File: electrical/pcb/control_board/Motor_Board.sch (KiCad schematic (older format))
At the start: 72 parts, among them J1 XT30-M, J10 Molex_172675-0613, J11 Molex_172675-0613, J12 TSW-104-07-F-T, J13 Molex_172675-0613, J14 Molex_172675-0613, J15 TSW-104-07-F-T, J16 ED2627-ND, J17 ED2627-ND, J18 ED2627-ND, J19 TSW-104-07-F-T, J2 XT30-F, J20 PEC08SAAN, J21 PPTC102LFBN-RC, J3 XT30-F, J4 XT30-F, J5 XT30-M, J6 ED2580-ND, J7 TSW-104-07-F-T, J8 Molex_172675-0613, J9 Molex_172675-0613, T1 test_point, T2 test_point, T3 test_point, T4 test_point, T5 test_point, T6 test_point, U1 INA260, U2 PCA9685, U3 D24V22Fx, U4 D24V150Fx, U5 DC7G3HWA, y1 rover_silkscreen

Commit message: Finished rev2 layout for motor board
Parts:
- added MH5, MH6, MH7, MH8: #6THRU-HOLE, JPL Robotics:#6THRU-HOLE, symbol JPL_Robotics_Lib:#6THRU-HOLE
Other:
- note added: "For mounting brain board"
- note added: "For mounting to to \nrover structure"
- moved on the sheet: MH1, MH2, MH3, MH4
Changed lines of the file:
@@
 L JPL_Robotics_Lib:#6THRU-HOLE MH1
 U 1 1 60953101
-P 2250 8850
-F 0 "MH1" H 2381 8850 30  0000 L CNN
-F 1 "#6THRU-HOLE" H 2250 8990 30  0001 C CNN
-F 2 "JPL Robotics:#6THRU-HOLE" H 2250 8940 30  0001 C CNN
-F 3 "" H 2250 8940 30  0001 C CNN
-	1    2250 8850
+P 1450 8900
+F 0 "MH1" H 1581 8900 30  0000 L CNN
+F 1 "#6THRU-HOLE" H 1450 9040 30  0001 C CNN
+F 2 "JPL Robotics:#6THRU-HOLE" H 1450 8990 30  0001 C CNN
+F 3 "" H 1450 8990 30  0001 C CNN
+	1    1450 8900
 	1    0    0    -1
 $EndComp
@@
 L JPL_Robotics_Lib:#6THRU-HOLE MH2
 U 1 1 60953107
-P 2250 9000
-F 0 "MH2" H 2381 9000 30  0000 L CNN
-F 1 "#6THRU-HOLE" H 2250 9140 30  0001 C CNN
-F 2 "JPL Robotics:#6THRU-HOLE" H 2250 9090 30  0001 C CNN
-F 3 "" H 2250 9090 30  0001 C CNN
-	1    2250 9000
+P 1450 9050
+F 0 "MH2" H 1581 9050 30  0000 L CNN
+F 1 "#6THRU-HOLE" H 1450 9190 30  0001 C CNN
+F 2 "JPL Robotics:#6THRU-HOLE" H 1450 9140 30  0001 C CNN
+F 3 "" H 1450 9140 30  0001 C CNN
+	1    1450 9050
 	1    0    0    -1
 $EndComp
@@
 L JPL_Robotics_Lib:#6THRU-HOLE MH3
 U 1 1 6095310D
-P 2250 9150
-F 0 "MH3" H 2381 9150 30  0000 L CNN
-F 1 "#6THRU-HOLE" H 2250 9290 30  0001 C CNN
-F 2 "JPL Robotics:#6THRU-HOLE" H 2250 9240 30  0001 C CNN
-F 3 "" H 2250 9240 30  0001 C CNN
-	1    2250 9150
+P 1450 9200
+F 0 "MH3" H 1581 9200 30  0000 L CNN
+F 1 "#6THRU-HOLE" H 1450 9340 30  0001 C CNN
+F 2 "JPL Robotics:#6THRU-HOLE" H 1450 9290 30  0001 C CNN
+F 3 "" H 1450 9290 30  0001 C CNN
+	1    1450 9200
 	1    0    0    -1
 $EndComp
@@
 L JPL_Robotics_Lib:#6THRU-HOLE MH4
 U 1 1 60953113
-P 2250 9300
-F 0 "MH4" H 2381 9300 30  0000 L CNN
-F 1 "#6THRU-HOLE" H 2250 9440 30  0001 C CNN
-F 2 "JPL Robotics:#6THRU-HOLE" H 2250 9390 30  0001 C CNN
-F 3 "" H 2250 9390 30  0001 C CNN
-	1    2250 9300
+P 1450 9350
+F 0 "MH4" H 1581 9350 30  0000 L CNN
+F 1 "#6THRU-HOLE" H 1450 9490 30  0001 C CNN
+F 2 "JPL Robotics:#6THRU-HOLE" H 1450 9440 30  0001 C CNN
+F 3 "" H 1450 9440 30  0001 C CNN
+	1    1450 9350
 	1    0    0    -1
 $EndComp
@@
 NoConn ~ 14250 6500
 NoConn ~ 14250 6600
+$Comp
+L JPL_Robotics_Lib:#6THRU-HOLE MH5
+U 1 1 625AC662
+P 2350 8900
+F 0 "MH5" H 2481 8900 30  0000 L CNN
+F 1 "#6THRU-HOLE" H 2350 9040 30  0001 C CNN
+F 2 "JPL Robotics:#6THRU-HOLE" H 2350 8990 30  0001 C CNN
+F 3 "" H 2350 8990 30  0001 C CNN
+	1    2350 8900
+	1    0    0    -1
+$EndComp
+$Comp
+L JPL_Robotics_Lib:#6THRU-HOLE MH6
+U 1 1 625AC668
+P 2350 9050
+F 0 "MH6" H 2481 9050 30  0000 L CNN
+F 1 "#6THRU-HOLE" H 2350 9190 30  0001 C CNN
+F 2 "JPL Robotics:#6THRU-HOLE" H 2350 9140 30  0001 C CNN
+F 3 "" H 2350 9140 30  0001 C CNN
+	1    2350 9050
+	1    0    0    -1
+$EndComp
+$Comp
+L JPL_Robotics_Lib:#6THRU-HOLE MH7
+U 1 1 625AC66E
+P 2350 9200
+F 0 "MH7" H 2481 9200 30  0000 L CNN
+F 1 "#6THRU-HOLE" H 2350 9340 30  0001 C CNN
+F 2 "JPL Robotics:#6THRU-HOLE" H 2350 9290 30  0001 C CNN
+F 3 "" H 2350 9290 30  0001 C CNN
+	1    2350 9200
+	1    0    0    -1
+$EndComp
+$Comp
+L JPL_Robotics_Lib:#6THRU-HOLE MH8
+U 1 1 625AC674
+P 2350 9350
+F 0 "MH8" H 2481 9350 30  0000 L CNN
+F 1 "#6THRU-HOLE" H 2350 9490 30  0001 C CNN
+F 2 "JPL Robotics:#6THRU-HOLE" H 2350 9440 30  0001 C CNN
+F 3 "" H 2350 9440 30  0001 C CNN
+	1    2350 9350
+	1    0    0    -1
+$EndComp
+Text Notes 1250 8800 0    31   ~ 0
+For mounting to to \nrover structure
+Text Notes 2100 8800 0    31   ~ 0
+For mounting brain board
 $EndSCHEMATC

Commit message: Some small updates before final routing
- Routed 12V_EN line to rpi
- A bunch of schematic cleanup
- Switched ESTOP LEDs to 5v from 3.3v
- Updated LED resistor sizing
- Connected available LEDs to unused rpi GPIOse
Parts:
- added R21: 0, symbol Device:R
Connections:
- wire segments 396 -> 398
- no-connect marks 67 -> 66
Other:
- note added: "Corner Steering \nServos Header"
- note added: "EN is pulled up by default on the \nD24V22F12, enabling it. Connect \nEN directly to RPi, so RPi can drive \nthis pin low and disable 12V output. \n\nThis resistor is a depop-able, just \nin case"
- note added: "Extra PWM Outputs Headers"
- note added: "Note: laid out the pins on this connector so that \nit wouldn’t be disastrous if the direction was \naccidentally switched"
- note added: "Note: leaving these unconnected, and \nsupplying +5V directly from the 5V bus"
- note added: "These are decoupling caps for the servos"
- note removed: "I think these are staying unconnected"
- note removed: "TODO: make sure to place this interboard connector such that no one will ever fuck up the direction this is plugged in"
- note removed: "TODO: think about A vs U naming convention"
- note removed: "TODO: tie EN pin for 12v reg to pin on the rpi. Also add a pull down for this\n\nEric to look into what we want to do here"
- note removed: "These are decoupling caps for the servos \n(todo: put as close to servos as possible in board layout)"
- moved on the sheet: C19, J19, J21, R10, R6, R7, R8, R9, U5

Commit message: Updates to layout
- Placed 12V_enable line in layout
- Placed additional LED resistors in layout
- Placed testpoints in layout
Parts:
- removed T5: test_point, TestPoint:TestPoint_Pad_1.0x1.0mm, symbol JPL_Robotics_Lib:test_point
- R2, R3, R4: symbol Device:R -> Device:R_US
- R21: footprint (none) -> Resistor_THT:R_Axial_DIN0207_L6.3mm_D2.5mm_P7.62mm_Horizontal; symbol Device:R -> Device:R_US
- renumbered T6 to T5
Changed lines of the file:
@@
 P 14650 9000
 AR Path="/60B753B5" Ref="T?"  Part="1"
-AR Path="/60A51BAC/60B753B5" Ref="T6"  Part="1"
-F 0 "T6" V 14650 8900 30  0000 L CNN
+AR Path="/60A51BAC/60B753B5" Ref="T5"  Part="1"
+F 0 "T5" V 14650 8900 30  0000 L CNN
 F 1 "test_point" H 14800 9250 50  0001 C CNN
 F 2 "TestPoint:TestPoint_Pad_1.0x1.0mm" H 14600 8950 50  0001 C CNN
@@
 Pulllups for e_stop signals
 $Comp
-L Device:R R2
+L Device:R_US R2
 U 1 1 61145EF5
 P 3150 3650
@@
 $EndComp
 $Comp
-L Device:R R3
+L Device:R_US R3
 U 1 1 6115BE1A
 P 3450 3650
@@
 $EndComp
 $Comp
-L Device:R R4
+L Device:R_US R4
 U 1 1 6115C337
 P 3750 3650
@@
 	1    13250 7650
 	1    0    0    -1
-$EndComp
-$Comp
-L JPL_Robotics_Lib:test_point T?
-U 1 1 6123BED4
-P 13200 9500
-AR Path="/6123BED4" Ref="T?"  Part="1"
-AR Path="/60A51BAC/6123BED4" Ref="T5"  Part="1"
-F 0 "T5" H 13150 9450 30  0000 L CNN
-F 1 "test_point" H 13350 9750 50  0001 C CNN
-F 2 "TestPoint:TestPoint_Pad_1.0x1.0mm" H 13150 9450 50  0001 C CNN
-F 3 "" H 13150 9450 50  0001 C CNN
-	1    13200 9500
-	-1   0    0    1
 $EndComp
 Text Notes 13750 5250 0    98   ~ 0
@@
 Wire Wire Line
 	14650 9150 14800 9150
-Connection ~ 13350 9500
 NoConn ~ 14500 9300
 Wire Wire Line
@@
 For mounting brain board
 $Comp
-L Device:R R21
+L Device:R_US R21
 U 1 1 62A1852A
 P 13200 9300
 F 0 "R21" V 12993 9300 50  0000 C CNN
 F 1 "0" V 13084 9300 50  0000 C CNN
-F 2 "" V 13130 9300 50  0001 C CNN
+F 2 "Resistor_THT:R_Axial_DIN0207_L6.3mm_D2.5mm_P7.62mm_Horizontal" V 13130 9300 50  0001 C CNN
 F 3 "~" H 13200 9300 50  0001 C CNN
 	1    13200 9300

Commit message: Add 277-11404-ND
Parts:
- J16, J17, J18: value ED2627-ND -> 277-11404-ND
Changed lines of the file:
@@
 AR Path="/60A51BAC/60B1CB30" Ref="J18"  Part="1"
 F 0 "J18" H 11050 3000 39  0000 L CNN
-F 1 "ED2627-ND" H 10919 3384 50  0001 C CNN
+F 1 "277-11404-ND" H 10919 3384 50  0001 C CNN
 F 2 "JPL Robotics:277-11404-ND" H 10800 3400 50  0001 C CNN
 F 3 "" H 10800 3400 50  0001 C CNN
@@
 AR Path="/60A51BAC/60B1CB18" Ref="J17"  Part="1"
 F 0 "J17" H 11050 2650 39  0000 L CNN
-F 1 "ED2627-ND" H 10919 3034 50  0001 C CNN
+F 1 "277-11404-ND" H 10919 3034 50  0001 C CNN
 F 2 "JPL Robotics:277-11404-ND" H 10800 3050 50  0001 C CNN
 F 3 "" H 10800 3050 50  0001 C CNN
@@
 AR Path="/60A51BAC/60B1CB0E" Ref="J16"  Part="1"
 F 0 "J16" H 11100 2300 39  0000 C CNN
-F 1 "ED2627-ND" H 10919 2684 50  0001 C CNN
+F 1 "277-11404-ND" H 10919 2684 50  0001 C CNN
 F 2 "JPL Robotics:277-11404-ND" H 10800 2700 50  0001 C CNN
 F 3 "" H 10800 2700 50  0001 C CNN

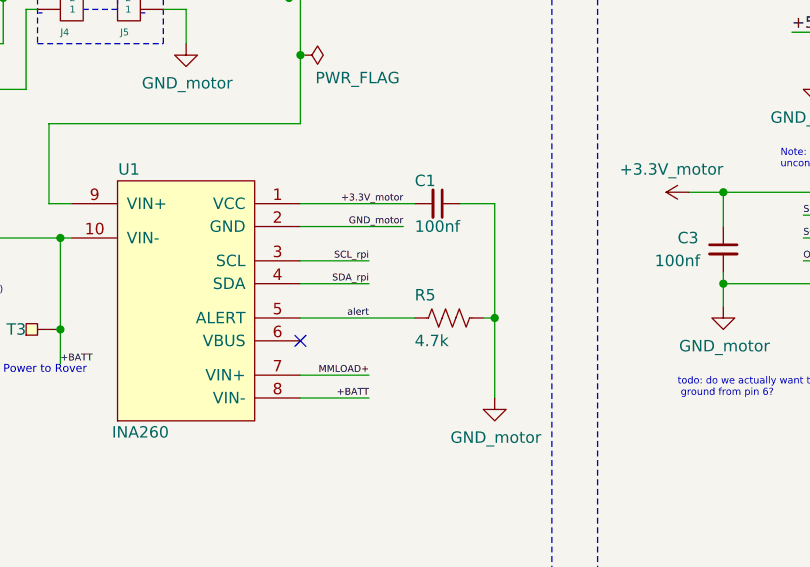
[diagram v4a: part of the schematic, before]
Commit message: Moved alert from pull-down to +3.3V pull-up
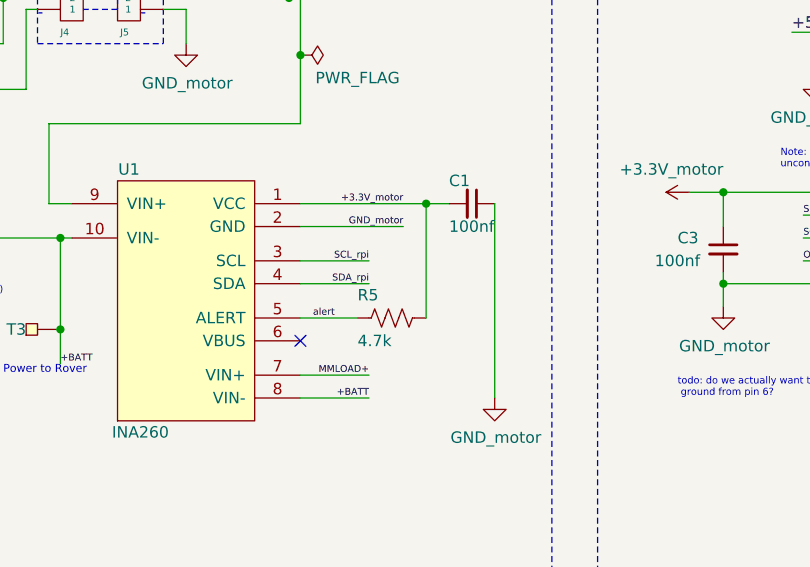
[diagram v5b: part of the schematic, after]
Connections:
- net +3.3V_motor: now also R5.1
- net GND_motor: no longer R5.1
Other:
- moved on the sheet: C1, R5
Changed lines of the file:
@@
 Wire Wire Line
 	3800 6800 4100 6800
-Wire Wire Line
-	4650 7050 4650 7400
-Wire Wire Line
-	4600 7050 4650 7050
-Wire Wire Line
-	4650 6550 4650 7050
-Wire Wire Line
-	4500 6550 4650 6550
-Wire Wire Line
-	3800 7050 4300 7050
-Wire Wire Line
-	3800 6550 4300 6550
 $Comp
 L JPL_Robotics_Lib:GND_motor #PWR06
@@
 L Device:C_Small C?
 U 1 1 61378A2A
-P 4400 6550
+P 4550 6550
 AR Path="/60A5279E/61378A2A" Ref="C?"  Part="1"
 AR Path="/60A51BAC/61378A2A" Ref="C1"  Part="1"
-F 0 "C1" V 4300 6450 50  0000 L CNN
-F 1 "100nf" V 4500 6450 50  0000 L CNN
-F 2 "Resistor_THT:R_Axial_DIN0207_L6.3mm_D2.5mm_P7.62mm_Horizontal" H 4400 6550 50  0001 C CNN
-F 3 "~" H 4400 6550 50  0001 C CNN
-	1    4400 6550
+F 0 "C1" V 4450 6450 50  0000 L CNN
+F 1 "100nf" V 4650 6450 50  0000 L CNN
+F 2 "Resistor_THT:R_Axial_DIN0207_L6.3mm_D2.5mm_P7.62mm_Horizontal" H 4550 6550 50  0001 C CNN
+F 3 "~" H 4550 6550 50  0001 C CNN
+	1    4550 6550
 	0    1    1    0
 $EndComp
@@
 L Device:R_US R?
 U 1 1 613B820D
-P 4450 7050
+P 4200 7050
 AR Path="/613B820D" Ref="R?"  Part="1"
 AR Path="/60A51BAC/613B820D" Ref="R5"  Part="1"
-F 0 "R5" V 4350 6900 50  0000 L CNN
-F 1 "4.7k" V 4550 6900 50  0000 L CNN
-F 2 "Resistor_THT:R_Axial_DIN0207_L6.3mm_D2.5mm_P7.62mm_Horizontal" V 4490 7040 50  0001 C CNN
-F 3 "~" H 4450 7050 50  0001 C CNN
-	1    4450 7050
+F 0 "R5" V 4100 6900 50  0000 L CNN
+F 1 "4.7k" V 4300 6900 50  0000 L CNN
+F 2 "Resistor_THT:R_Axial_DIN0207_L6.3mm_D2.5mm_P7.62mm_Horizontal" V 4240 7040 50  0001 C CNN
+F 3 "~" H 4200 7050 50  0001 C CNN
+	1    4200 7050
 	0    1    1    0
 $EndComp
 Text Label 4250 6550 2    30   ~ 0
 +3.3V_motor
-Text Label 4100 7050 2    30   ~ 0
+Text Label 3950 7050 2    30   ~ 0
 alert
 Text Label 4100 6900 2    30   ~ 0
@@
 Wire Wire Line
 	3300 5850 3300 5700
-Connection ~ 4650 7050
 Wire Wire Line
 	1900 6550 1900 6850
@@
 Wire Notes Line
 	12100 9900 12100 7000
+Wire Wire Line
+	4650 6550 4650 7400
+Wire Wire Line
+	4050 7050 3800 7050
+Wire Wire Line
+	3800 6550 4350 6550
+Wire Wire Line
+	4350 7050 4350 6550
+Connection ~ 4350 6550
+Wire Wire Line
+	4350 6550 4450 6550
 $EndSCHEMATC

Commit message: Update c19, c25, c27, c28 to polarized footprint
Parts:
- C19, C25, C27, C28: footprint Resistor_THT:R_Axial_DIN0207_L6.3mm_D2.5mm_P7.62mm_Horizontal -> Capacitor_THT:CP_Radial_D8.0mm_P3.80mm
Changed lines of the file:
@@
 F 0 "C19" V 9400 6250 50  0000 L CNN
 F 1 "100uf" V 9200 6250 50  0000 L CNN
-F 2 "Resistor_THT:R_Axial_DIN0207_L6.3mm_D2.5mm_P7.62mm_Horizontal" H 9300 6300 50  0001 C CNN
+F 2 "Capacitor_THT:CP_Radial_D8.0mm_P3.80mm" H 9300 6300 50  0001 C CNN
 F 3 "~" H 9300 6300 50  0001 C CNN
 	1    9300 6300
@@
 F 0 "C25" V 10250 9400 50  0000 L CNN
 F 1 "100uf" V 10050 9400 50  0000 L CNN
-F 2 "Resistor_THT:R_Axial_DIN0207_L6.3mm_D2.5mm_P7.62mm_Horizontal" H 10150 9450 50  0001 C CNN
+F 2 "Capacitor_THT:CP_Radial_D8.0mm_P3.80mm" H 10150 9450 50  0001 C CNN
 F 3 "~" H 10150 9450 50  0001 C CNN
 	1    10150 9450
@@
 F 0 "C27" V 10550 9400 50  0000 L CNN
 F 1 "100uf" V 10350 9400 50  0000 L CNN
-F 2 "Resistor_THT:R_Axial_DIN0207_L6.3mm_D2.5mm_P7.62mm_Horizontal" H 10450 9450 50  0001 C CNN
+F 2 "Capacitor_THT:CP_Radial_D8.0mm_P3.80mm" H 10450 9450 50  0001 C CNN
 F 3 "~" H 10450 9450 50  0001 C CNN
 	1    10450 9450
@@
 F 0 "C28" V 10850 9400 50  0000 L CNN
 F 1 "100uf" V 10650 9400 50  0000 L CNN
-F 2 "Resistor_THT:R_Axial_DIN0207_L6.3mm_D2.5mm_P7.62mm_Horizontal" H 10750 9450 50  0001 C CNN
+F 2 "Capacitor_THT:CP_Radial_D8.0mm_P3.80mm" H 10750 9450 50  0001 C CNN
 F 3 "~" H 10750 9450 50  0001 C CNN
 	1    10750 9450

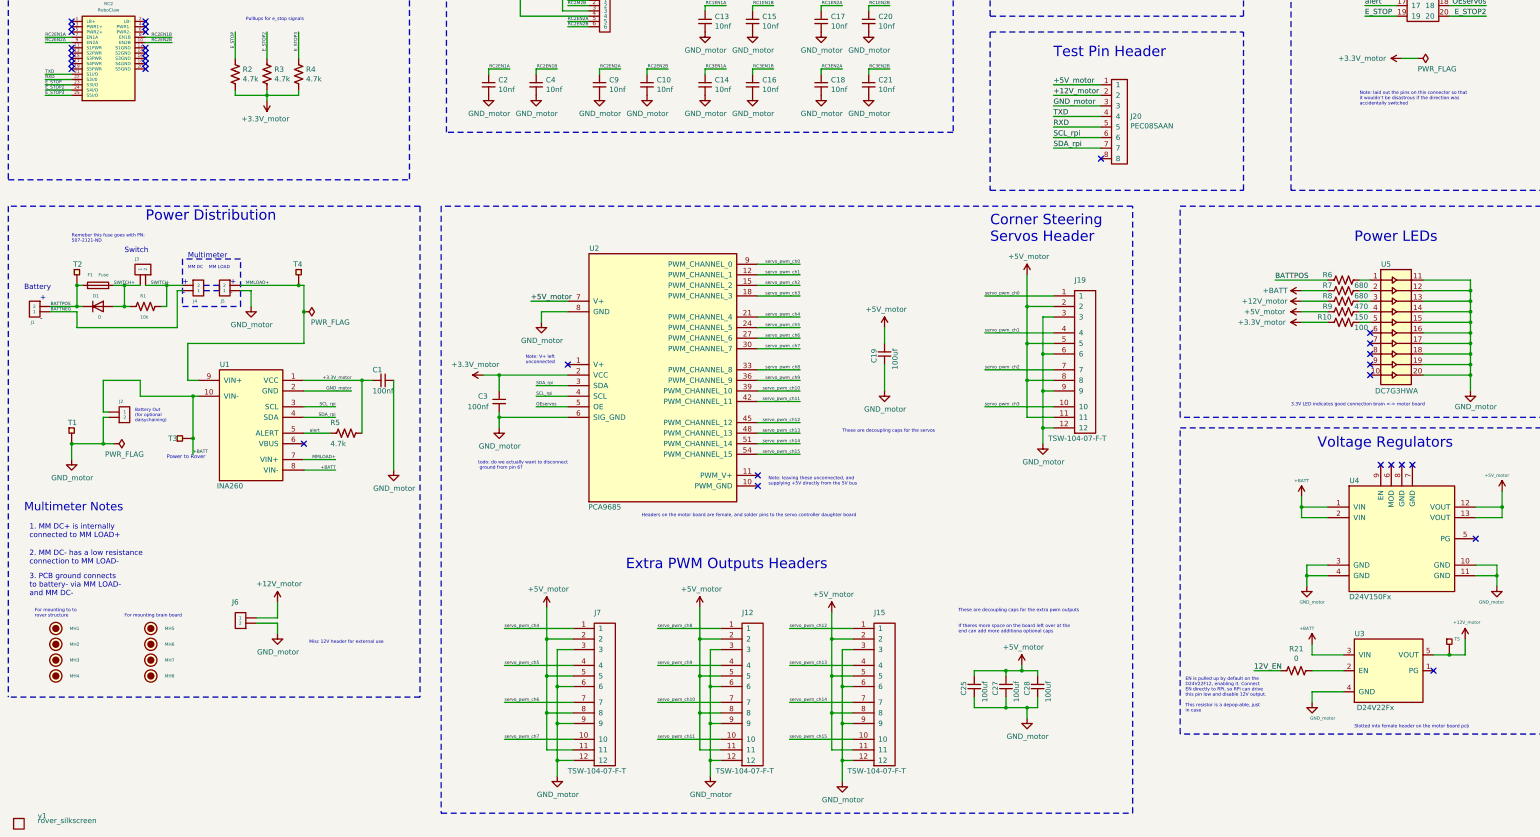
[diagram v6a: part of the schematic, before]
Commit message: Refactor the test points, in particular added an array of test points for motor board. Add a couple of bigger test point footprints as well
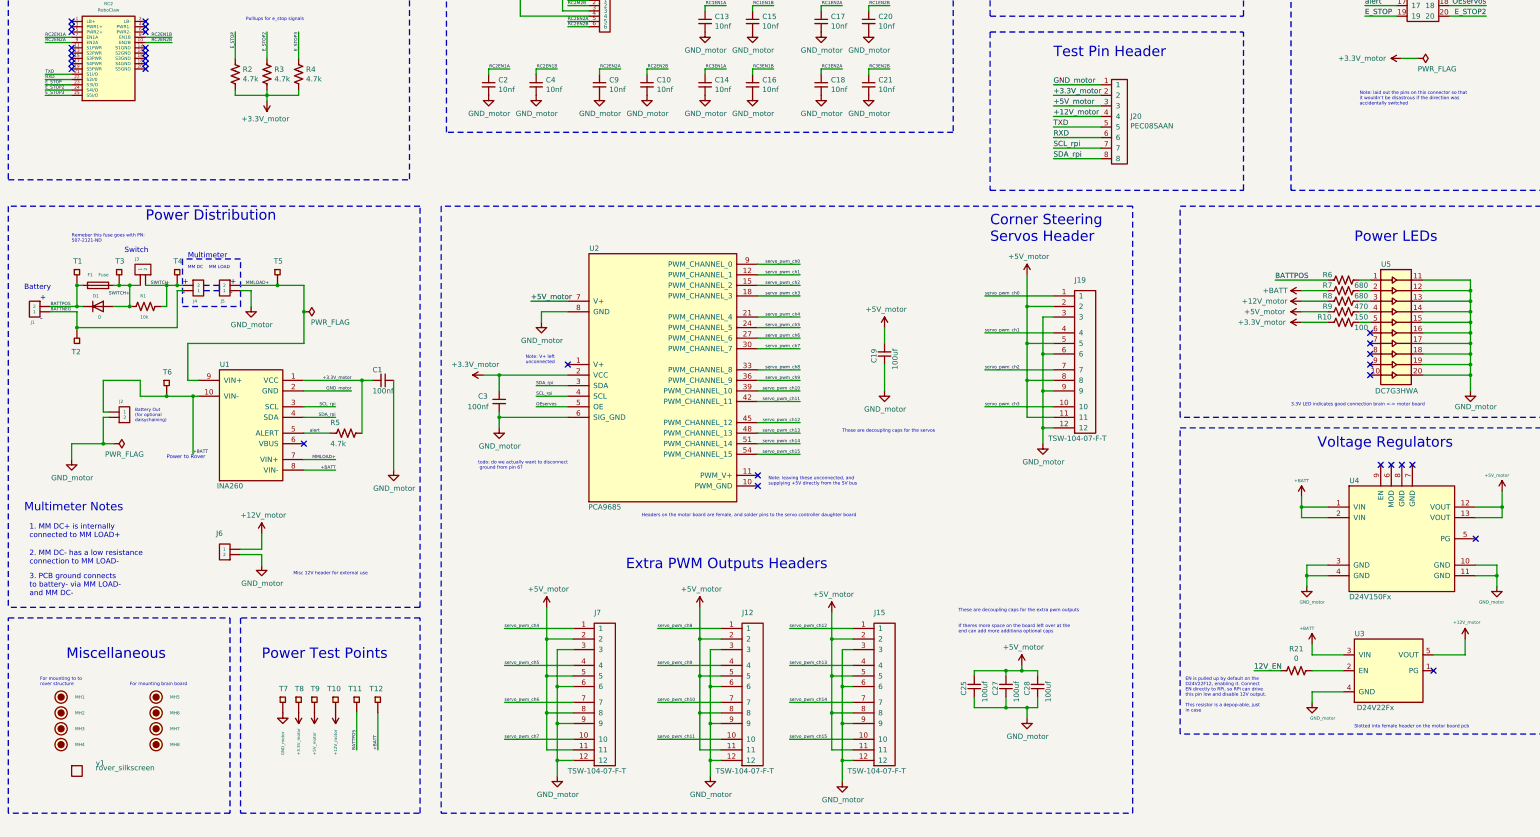
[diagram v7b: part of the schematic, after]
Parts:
- added T10, T11, T12, T8, T9: JPL Robotics:test_point_hole, symbol JPL_Robotics_Lib:test_point
- added T6: test_point, JPL Robotics:test_point, symbol JPL_Robotics_Lib:test_point
- added T7: test_point, JPL Robotics:test_point_hole, symbol JPL_Robotics_Lib:test_point
- T1, T2: footprint TestPoint:TestPoint_Pad_1.0x1.0mm -> JPL Robotics:test_point
- T3, T4, T5: value test_point -> JPL Robotics:test_point; footprint TestPoint:TestPoint_Pad_1.0x1.0mm -> (none)
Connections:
- net +12V_motor: now also J20.4, T10.1; no longer J20.2, T5.1
- net +3.3V_motor: now also J20.2, T8.1
- net +5V_motor: now also J20.3, T9.1; no longer J20.1
- net +BATT: now also T12.1, T6.1; no longer T3.1
- net BATTNEG: now also T2.1
- net BATTPOS: now also T1.1, T11.1; no longer T2.1
- net GND_motor: now also J20.1, T7.1; no longer J20.3, T1.1
- net MMLOAD+: now also T5.1; no longer T4.1
- net RXD: now also J20.6; no longer J20.5
- net SCL_rpi: now also J20.7; no longer J20.6
- net SDA_rpi: now also J20.8; no longer J20.7
- net SWITCH+: now also T3.1
- net SWITCH-: now also T4.1
- net TXD: now also J20.5; no longer J20.4
- no-connect marks 66 -> 65
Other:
- note added: "Miscellaneous"
- note added: "Power Test Points"
- moved on the sheet: J6, MH1, MH2, MH3, MH4, MH5, MH6, MH7, MH8, y1
